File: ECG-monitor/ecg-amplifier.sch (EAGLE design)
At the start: 21 parts, among them IC1 OPA2333D, IC2 OPA2333D, IC3 OPA2333D, IC5 OPA333D

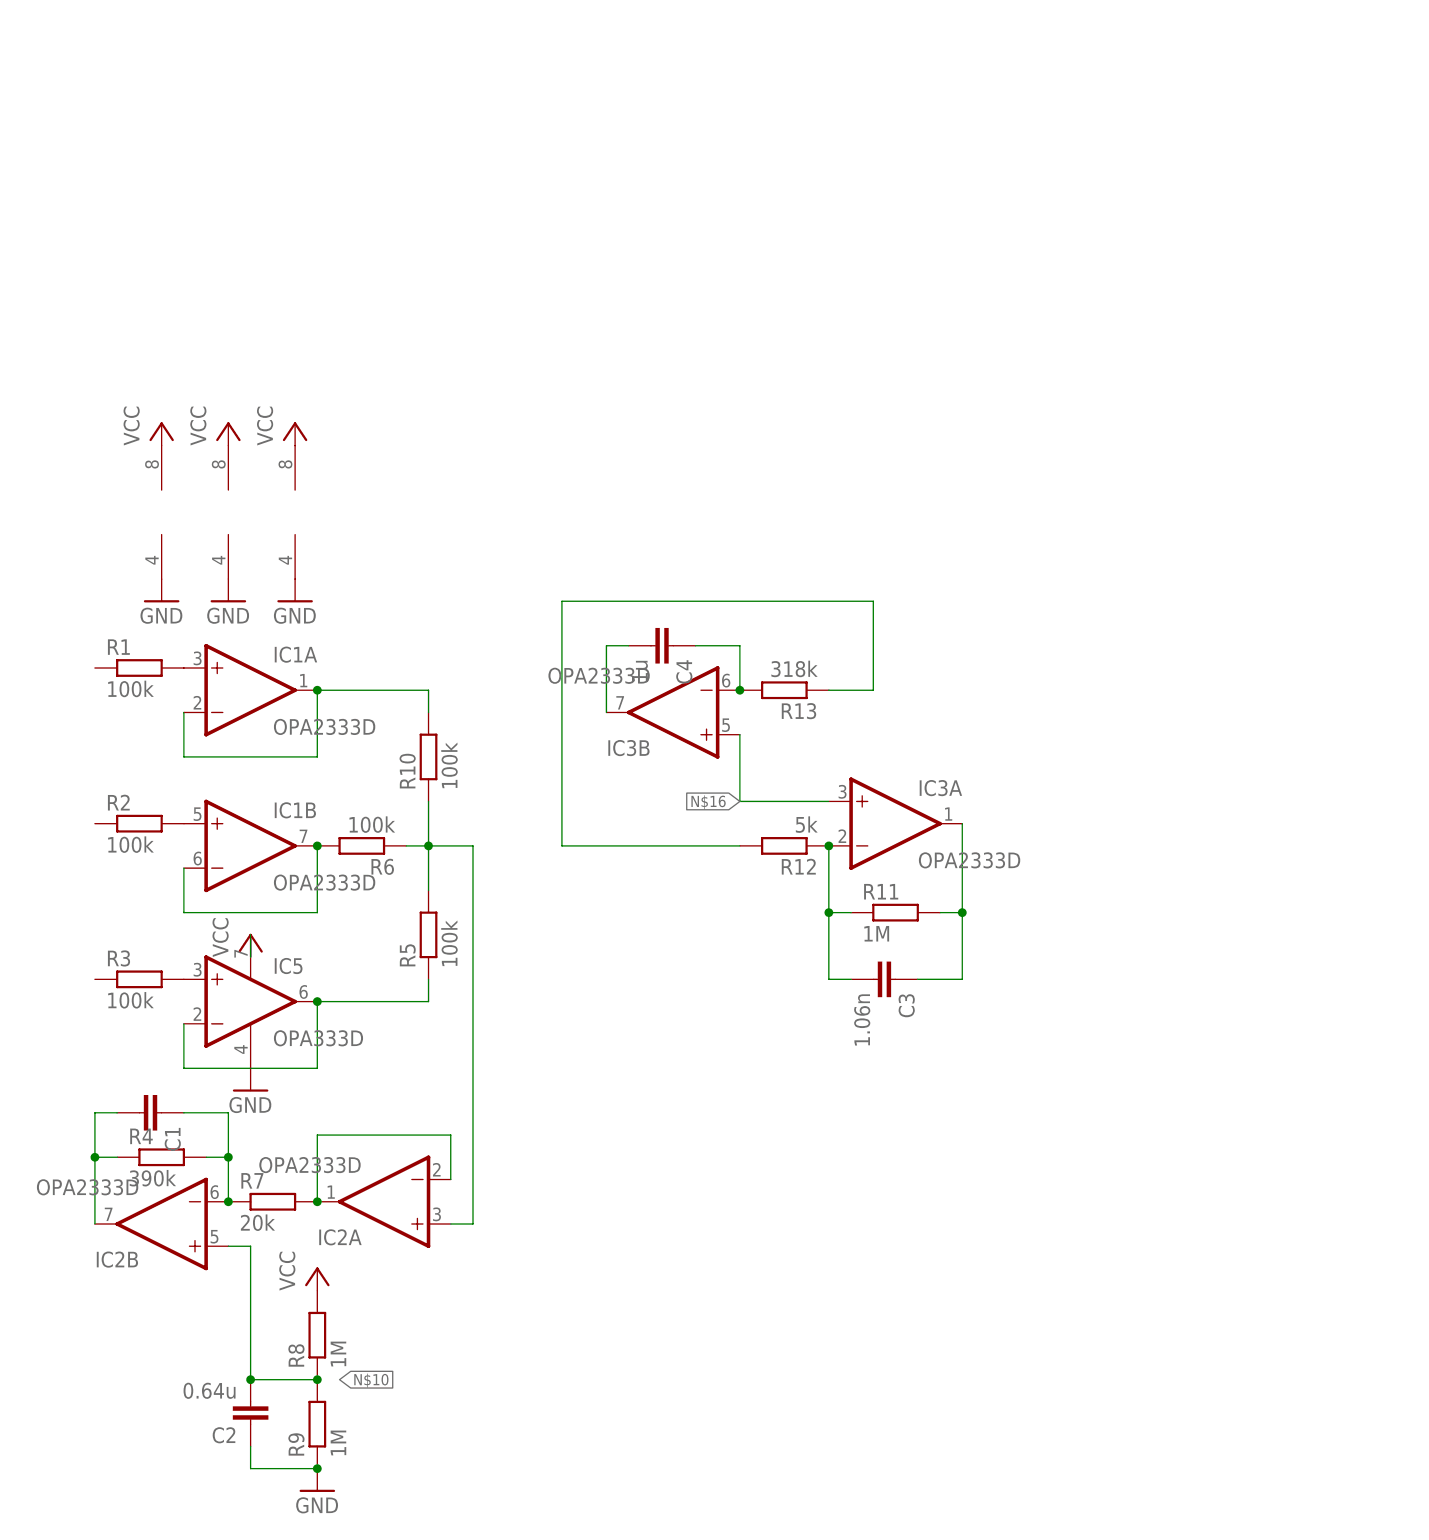
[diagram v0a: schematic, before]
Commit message: found eagle part for teensy-lc and bluetooth module
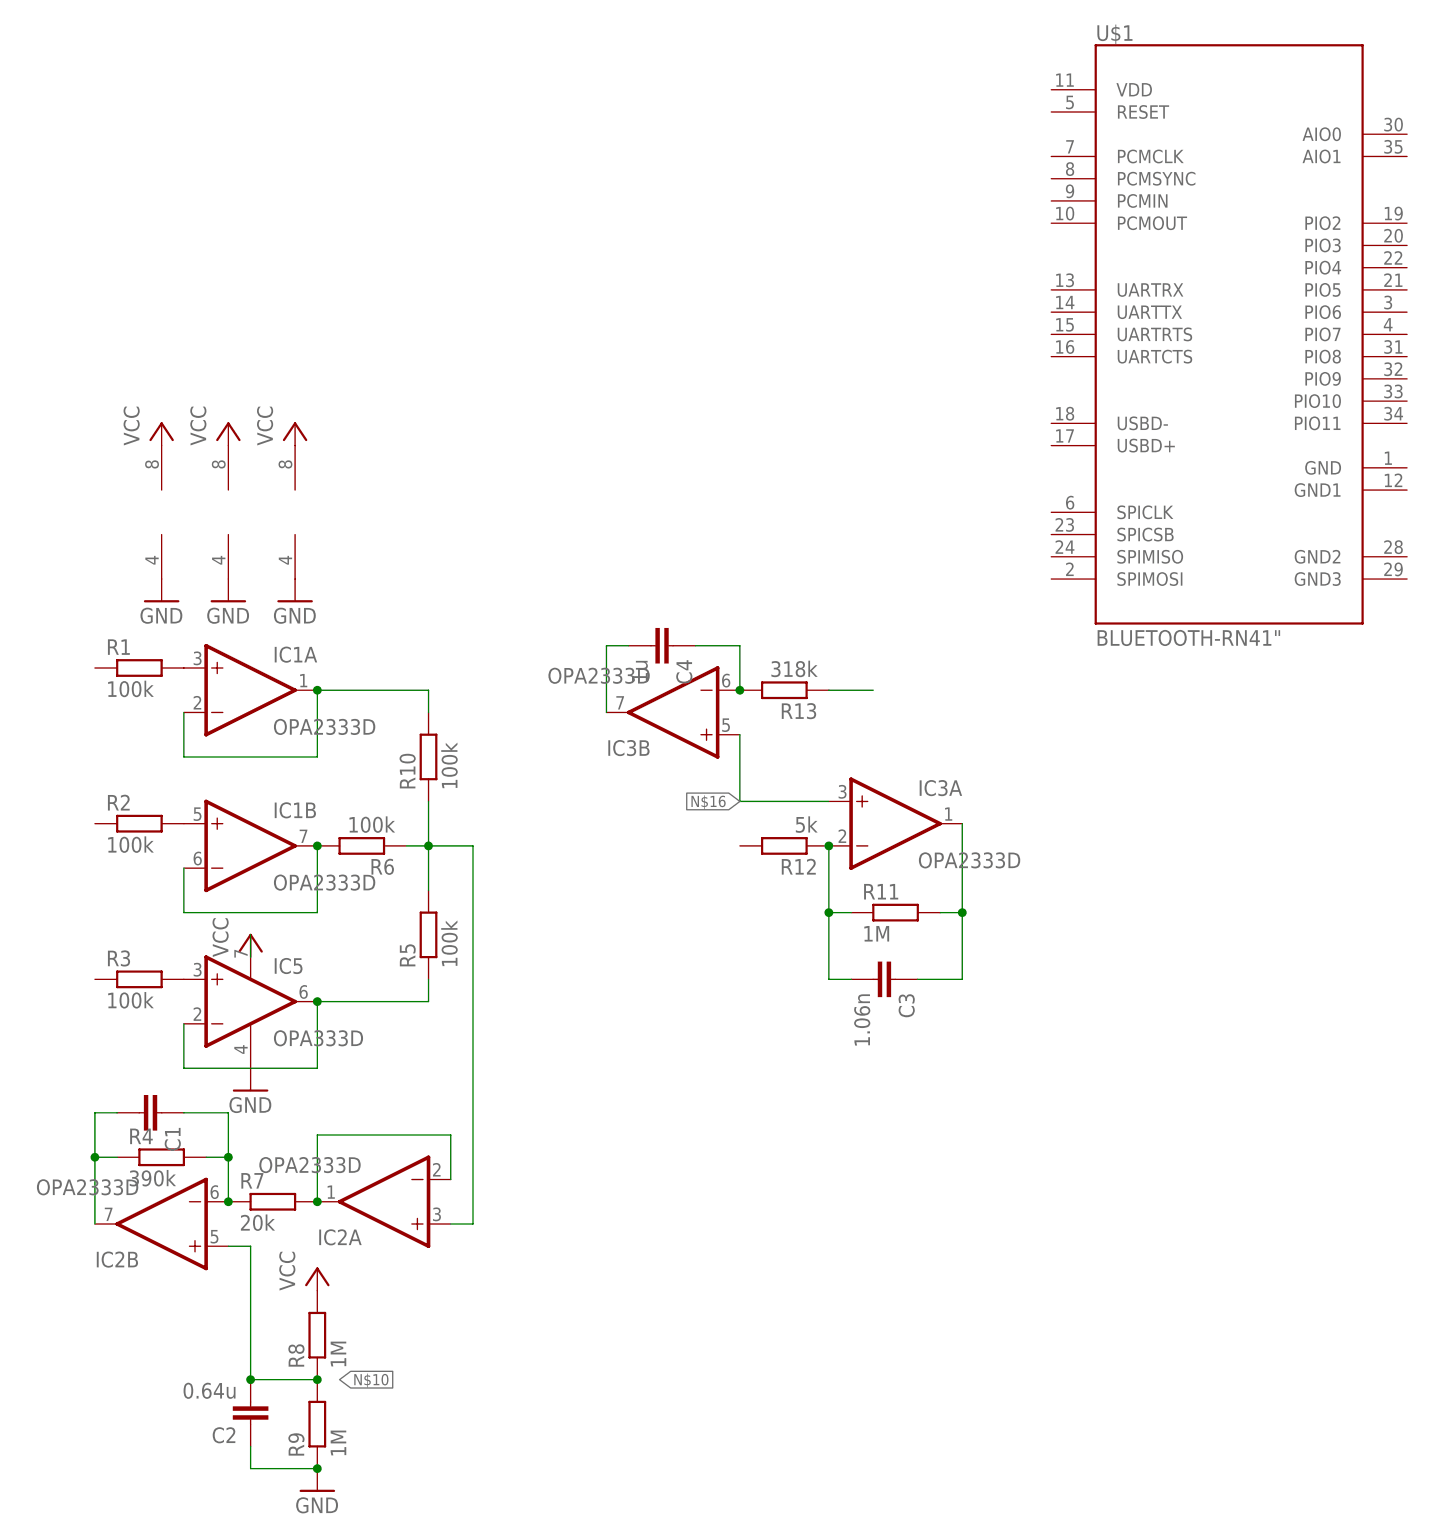
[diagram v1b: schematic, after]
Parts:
- added U$1: BLUETOOTH-RN41", SparkFun-RF:BLUETOOTH-RN41"
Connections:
- removed net N$17: R12.2, R13.1
- new net N$18: R13.1
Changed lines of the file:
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@@
 <layer number="48" name="Document" color="7" fill="1" visible="no" active="no"/>
 <layer number="49" name="Reference" color="7" fill="1" visible="no" active="no"/>
+<layer number="50" name="dxf" color="7" fill="1" visible="no" active="no"/>
 <layer number="51" name="tDocu" color="6" fill="1" visible="no" active="no"/>
 <layer number="52" name="bDocu" color="7" fill="1" visible="no" active="no"/>
+<layer number="53" name="tGND_GNDA" color="7" fill="9" visible="no" active="no"/>
+<layer number="54" name="bGND_GNDA" color="1" fill="9" visible="no" active="no"/>
+<layer number="56" name="wert" color="7" fill="1" visible="no" active="no"/>
+<layer number="57" name="tCAD" color="7" fill="1" visible="no" active="no"/>
 <layer number="90" name="Modules" color="5" fill="1" visible="yes" active="yes"/>
 <layer number="91" name="Nets" color="2" fill="1" visible="yes" active="yes"/>
@@
 <layer number="98" name="Guide" color="6" fill="1" visible="yes" active="yes"/>
 <layer number="99" name="SpiceOrder" color="5" fill="1" visible="yes" active="yes"/>
+<layer number="100" name="Muster" color="7" fill="1" visible="no" active="no"/>
+<layer number="101" name="Patch_Top" color="12" fill="4" visible="yes" active="yes"/>
+<layer number="102" name="Vscore" color="7" fill="1" visible="yes" active="yes"/>
+<layer number="103" name="tMap" color="7" fill="1" visible="yes" active="yes"/>
+<layer number="104" name="Name" color="16" fill="1" visible="yes" active="yes"/>
+<layer number="105" name="tPlate" color="7" fill="1" visible="yes" active="yes"/>
+<layer number="106" name="bPlate" color="7" fill="1" visible="yes" active="yes"/>
+<layer number="107" name="Crop" color="7" fill="1" visible="yes" active="yes"/>
+<layer number="108" name="tplace-old" color="10" fill="1" visible="yes" active="yes"/>
+<layer number="109" name="ref-old" color="11" fill="1" visible="yes" active="yes"/>
+<layer number="110" name="fp0" color="7" fill="1" visible="yes" active="yes"/>
+<layer number="111" name="LPC17xx" color="7" fill="1" visible="yes" active="yes"/>
+<layer number="112" name="tSilk" color="7" fill="1" visible="yes" active="yes"/>
+<layer number="113" name="IDFDebug" color="4" fill="1" visible="yes" active="yes"/>
+<layer number="116" name="Patch_BOT" color="9" fill="4" visible="yes" active="yes"/>
+<layer number="121" name="_tsilk" color="7" fill="1" visible="yes" active="yes"/>
+<layer number="122" name="_bsilk" color="7" fill="1" visible="yes" active="yes"/>
+<layer number="123" name="tTestmark" color="7" fill="1" visible="yes" active="yes"/>
+<layer number="124" name="bTestmark" color="7" fill="1" visible="yes" active="yes"/>
+<layer number="125" name="_tNames" color="7" fill="1" visible="yes" active="yes"/>
+<layer number="126" name="_bNames" color="7" fill="1" visible="yes" active="yes"/>
+<layer number="127" name="_tValues" color="7" fill="1" visible="yes" active="yes"/>
+<layer number="128" name="_bValues" color="7" fill="1" visible="yes" active="yes"/>
+<layer number="131" name="tAdjust" color="7" fill="1" visible="yes" active="yes"/>
+<layer number="132" name="bAdjust" color="7" fill="1" visible="yes" active="yes"/>
+<layer number="144" name="Drill_legend" color="7" fill="1" visible="yes" active="yes"/>
+<layer number="150" name="Notes" color="7" fill="1" visible="yes" active="yes"/>
+<layer number="151" name="HeatSink" color="7" fill="1" visible="yes" active="yes"/>
+<layer number="152" name="_bDocu" color="7" fill="1" visible="yes" active="yes"/>
+<layer number="153" name="FabDoc1" color="7" fill="1" visible="yes" active="yes"/>
+<layer number="154" name="FabDoc2" color="7" fill="1" visible="yes" active="yes"/>
+<layer number="155" name="FabDoc3" color="7" fill="1" visible="yes" active="yes"/>
+<layer number="199" name="Contour" color="7" fill="1" visible="yes" active="yes"/>
+<layer number="200" name="200bmp" color="1" fill="10" visible="yes" active="yes"/>
+<layer number="201" name="201bmp" color="2" fill="10" visible="yes" active="yes"/>
+<layer number="202" name="202bmp" color="3" fill="10" visible="yes" active="yes"/>
+<layer number="203" name="203bmp" color="4" fill="10" visible="yes" active="yes"/>
+<layer number="204" name="204bmp" color="5" fill="10" visible="yes" active="yes"/>
+<layer number="205" name="205bmp" color="6" fill="10" visible="yes" active="yes"/>
+<layer number="206" name="206bmp" color="7" fill="10" visible="yes" active="yes"/>
+<layer number="207" name="207bmp" color="8" fill="10" visible="yes" active="yes"/>
+<layer number="208" name="208bmp" color="9" fill="10" visible="yes" active="yes"/>
+<layer number="209" name="209bmp" color="7" fill="1" visible="yes" active="yes"/>
+<layer number="210" name="210bmp" color="7" fill="1" visible="yes" active="yes"/>
+<layer number="211" name="211bmp" color="7" fill="1" visible="yes" active="yes"/>
+<layer number="212" name="212bmp" color="7" fill="1" visible="yes" active="yes"/>
+<layer number="213" name="213bmp" color="7" fill="1" visible="yes" active="yes"/>
+<layer number="214" name="214bmp" color="7" fill="1" visible="yes" active="yes"/>
+<layer number="215" name="215bmp" color="7" fill="1" visible="yes" active="yes"/>
+<layer number="216" name="216bmp" color="7" fill="1" visible="yes" active="yes"/>
+<layer number="217" name="217bmp" color="18" fill="1" visible="no" active="no"/>
+<layer number="218" name="218bmp" color="19" fill="1" visible="no" active="no"/>
+<layer number="219" name="219bmp" color="20" fill="1" visible="no" active="no"/>
+<layer number="220" name="220bmp" color="21" fill="1" visible="no" active="no"/>
+<layer number="221" name="221bmp" color="22" fill="1" visible="no" active="no"/>
+<layer number="222" name="222bmp" color="23" fill="1" visible="no" active="no"/>
+<layer number="223" name="223bmp" color="24" fill="1" visible="no" active="no"/>
+<layer number="224" name="224bmp" color="25" fill="1" visible="no" active="no"/>
+<layer number="248" name="Housing" color="7" fill="1" visible="yes" active="yes"/>
+<layer number="249" name="Edge" color="7" fill="1" visible="yes" active="yes"/>
+<layer number="250" name="Descript" color="3" fill="1" visible="no" active="no"/>
+<layer number="251" name="SMDround" color="12" fill="11" visible="no" active="no"/>
+<layer number="254" name="cooling" color="7" fill="1" visible="yes" active="yes"/>
 </layers>
 <schematic xreflabel="%F%N/%S.%C%R" xrefpart="/%S.%C%R">
@@
 <part name="R12" library="eagle-ltspice" deviceset="R" device="" value="5k"/>
 <part name="R13" library="eagle-ltspice" deviceset="R" device="" value="318k"/>
+<part name="U$1" library="SparkFun-RF" deviceset="BLUETOOTH-RN41" device="&quot;"/>
 </parts>
 <sheets>
@@
 <instance part="R12" gate="G$1" x="91.44" y="60.96" rot="R180"/>
 <instance part="R13" gate="G$1" x="91.44" y="78.74" rot="R180"/>
+<instance part="U$1" gate="G$1" x="142.24" y="119.38"/>
 </instances>
 <busses>
@@
 </segment>
 </net>
-<net name="N$17" class="0">
+<net name="N$18" class="0">
 <segment>
 <pinref part="R13" gate="G$1" pin="1"/>
 <wire x1="96.52" y1="78.74" x2="101.6" y2="78.74" width="0.1524" layer="91"/>
-<wire x1="101.6" y1="78.74" x2="101.6" y2="88.9" width="0.1524" layer="91"/>
-<wire x1="101.6" y1="88.9" x2="66.04" y2="88.9" width="0.1524" layer="91"/>
-<wire x1="66.04" y1="88.9" x2="66.04" y2="60.96" width="0.1524" layer="91"/>
-<pinref part="R12" gate="G$1" pin="2"/>
-<wire x1="66.04" y1="60.96" x2="86.36" y2="60.96" width="0.1524" layer="91"/>
-</segment>
-</net>
+</segment>
+</net>
